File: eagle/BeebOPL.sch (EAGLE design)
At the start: 46 parts, among them IC1 LM324N, IC2 YM3014B, IC3 LM7805, IC5 74LS02N, IC6 YM3812, IC7 74LS04N, IC9 74HCT688N, J1 1 MHz Bus, J2 Feed-through, J3 3.5mm Jack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

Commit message: Further refined schematic
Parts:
- added C10, C11: 10nF, resistor:C-EU050-024X044
- JP3: value (none) -> AUDIO
- JP4: value (none) -> LED
- JP5: value (none) -> PWR
- S2: device SparkFun-Retired:JUMPER-2PTH -> SparkFun-Retired:SOLDERJUMPERTRACE-PTH
- S3: value JUMPER-3PTH -> REG; device SparkFun-Retired:JUMPER-3PTH -> YMSynth:J2
- TR1: value IRFD9024DIL -> IRFD9024; device YMSynth:IRFD9024DIL -> YMSynth:IRFD9024-OPTN
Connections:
- new net N$29: S3.1, TR1.S
- new net N$4: J4.PWR, JP5.4, TR1.D
- new net YM/IRQ: IC6./IRQ, S2.2
- net /IRQ: no longer IC6./IRQ, S2.2
- net GND: now also C10.2, C11.2
- net VCC: now also C10.1, C11.1; no longer J4.PWR, JP5.4, S3.1, TR1.D, TR1.S
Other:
- note removed: "Make sure signals pass through links correctly"
- moved on the sheet: C6, C7, S3

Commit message: Perfecting schematic
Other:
- note added: "Divide track to use voltage regulator"
- note removed: "Divide track to use power regulator"
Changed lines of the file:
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@@
 <grid distance="0.05" unitdist="inch" unit="inch" style="lines" multiple="1" display="no" altdistance="0.01" altunitdist="inch" altunit="inch"/>
 <layers>
-<layer number="1" name="Top" color="4" fill="1" visible="yes" active="no"/>
-<layer number="16" name="Bottom" color="1" fill="1" visible="yes" active="no"/>
-<layer number="17" name="Pads" color="2" fill="1" visible="yes" active="no"/>
-<layer number="18" name="Vias" color="2" fill="1" visible="yes" active="no"/>
-<layer number="19" name="Unrouted" color="6" fill="1" visible="yes" active="no"/>
-<layer number="20" name="Dimension" color="15" fill="1" visible="yes" active="no"/>
-<layer number="21" name="tPlace" color="7" fill="1" visible="yes" active="no"/>
-<layer number="22" name="bPlace" color="7" fill="1" visible="yes" active="no"/>
-<layer number="23" name="tOrigins" color="15" fill="1" visible="yes" active="no"/>
-<layer number="24" name="bOrigins" color="15" fill="1" visible="yes" active="no"/>
-<layer number="25" name="tNames" color="7" fill="1" visible="yes" active="no"/>
-<layer number="26" name="bNames" color="7" fill="1" visible="yes" active="no"/>
-<layer number="27" name="tValues" color="7" fill="1" visible="yes" active="no"/>
-<layer number="28" name="bValues" color="7" fill="1" visible="yes" active="no"/>
+<layer number="1" name="Top" color="4" fill="1" visible="no" active="no"/>
+<layer number="16" name="Bottom" color="1" fill="1" visible="no" active="no"/>
+<layer number="17" name="Pads" color="2" fill="1" visible="no" active="no"/>
+<layer number="18" name="Vias" color="2" fill="1" visible="no" active="no"/>
+<layer number="19" name="Unrouted" color="6" fill="1" visible="no" active="no"/>
+<layer number="20" name="Dimension" color="15" fill="1" visible="no" active="no"/>
+<layer number="21" name="tPlace" color="7" fill="1" visible="no" active="no"/>
+<layer number="22" name="bPlace" color="7" fill="1" visible="no" active="no"/>
+<layer number="23" name="tOrigins" color="15" fill="1" visible="no" active="no"/>
+<layer number="24" name="bOrigins" color="15" fill="1" visible="no" active="no"/>
+<layer number="25" name="tNames" color="7" fill="1" visible="no" active="no"/>
+<layer number="26" name="bNames" color="7" fill="1" visible="no" active="no"/>
+<layer number="27" name="tValues" color="7" fill="1" visible="no" active="no"/>
+<layer number="28" name="bValues" color="7" fill="1" visible="no" active="no"/>
 <layer number="29" name="tStop" color="7" fill="3" visible="no" active="no"/>
 <layer number="30" name="bStop" color="7" fill="6" visible="no" active="no"/>
@@
 <layer number="35" name="tGlue" color="7" fill="4" visible="no" active="no"/>
 <layer number="36" name="bGlue" color="7" fill="5" visible="no" active="no"/>
-<layer number="37" name="tTest" color="7" fill="1" visible="yes" active="no"/>
-<layer number="38" name="bTest" color="7" fill="1" visible="yes" active="no"/>
+<layer number="37" name="tTest" color="7" fill="1" visible="no" active="no"/>
+<layer number="38" name="bTest" color="7" fill="1" visible="no" active="no"/>
 <layer number="39" name="tKeepout" color="4" fill="11" visible="no" active="no"/>
 <layer number="40" name="bKeepout" color="1" fill="11" visible="no" active="no"/>
@@
 <layer number="44" name="Drills" color="7" fill="1" visible="no" active="no"/>
 <layer number="45" name="Holes" color="7" fill="1" visible="no" active="no"/>
-<layer number="46" name="Milling" color="3" fill="1" visible="yes" active="no"/>
-<layer number="47" name="Measures" color="7" fill="1" visible="yes" active="no"/>
-<layer number="48" name="Document" color="7" fill="1" visible="yes" active="no"/>
-<layer number="49" name="Reference" color="7" fill="1" visible="yes" active="no"/>
-<layer number="50" name="dxf" color="7" fill="1" visible="yes" active="no"/>
-<layer number="51" name="tDocu" color="7" fill="1" visible="yes" active="no"/>
-<layer number="52" name="bDocu" color="7" fill="1" visible="yes" active="no"/>
-<layer number="53" name="tGND_GNDA" color="7" fill="9" visible="yes" active="no"/>
-<layer number="54" name="bGND_GNDA" color="1" fill="9" visible="yes" active="no"/>
-<layer number="56" name="wert" color="7" fill="1" visible="yes" active="no"/>
-<layer number="57" name="tCAD" color="7" fill="1" visible="yes" active="no"/>
-<layer number="59" name="tCarbon" color="7" fill="1" visible="yes" active="no"/>
-<layer number="60" name="bCarbon" color="7" fill="1" visible="yes" active="no"/>
+<layer number="46" name="Milling" color="3" fill="1" visible="no" active="no"/>
+<layer number="47" name="Measures" color="7" fill="1" visible="no" active="no"/>
+<layer number="48" name="Document" color="7" fill="1" visible="no" active="no"/>
+<layer number="49" name="Reference" color="7" fill="1" visible="no" active="no"/>
+<layer number="50" name="dxf" color="7" fill="1" visible="no" active="no"/>
+<layer number="51" name="tDocu" color="7" fill="1" visible="no" active="no"/>
+<layer number="52" name="bDocu" color="7" fill="1" visible="no" active="no"/>
+<layer number="53" name="tGND_GNDA" color="7" fill="9" visible="no" active="no"/>
+<layer number="54" name="bGND_GNDA" color="1" fill="9" visible="no" active="no"/>
+<layer number="56" name="wert" color="7" fill="1" visible="no" active="no"/>
+<layer number="57" name="tCAD" color="7" fill="1" visible="no" active="no"/>
+<layer number="59" name="tCarbon" color="7" fill="1" visible="no" active="no"/>
+<layer number="60" name="bCarbon" color="7" fill="1" visible="no" active="no"/>
 <layer number="90" name="Modules" color="5" fill="1" visible="yes" active="yes"/>
 <layer number="91" name="Nets" color="2" fill="1" visible="yes" active="yes"/>
@@
 <text x="-175.26" y="-175.26" size="10.16" layer="97" font="vector">DATE: 29 Sept 2016</text>
 <text x="-88.9" y="-50.8" size="1.778" layer="97">Divide track to use
-power regulator</text>
+voltage regulator</text>
 <text x="-97.79" y="-109.22" size="1.778" layer="97">Divide track to use
 power MOSFET</text>

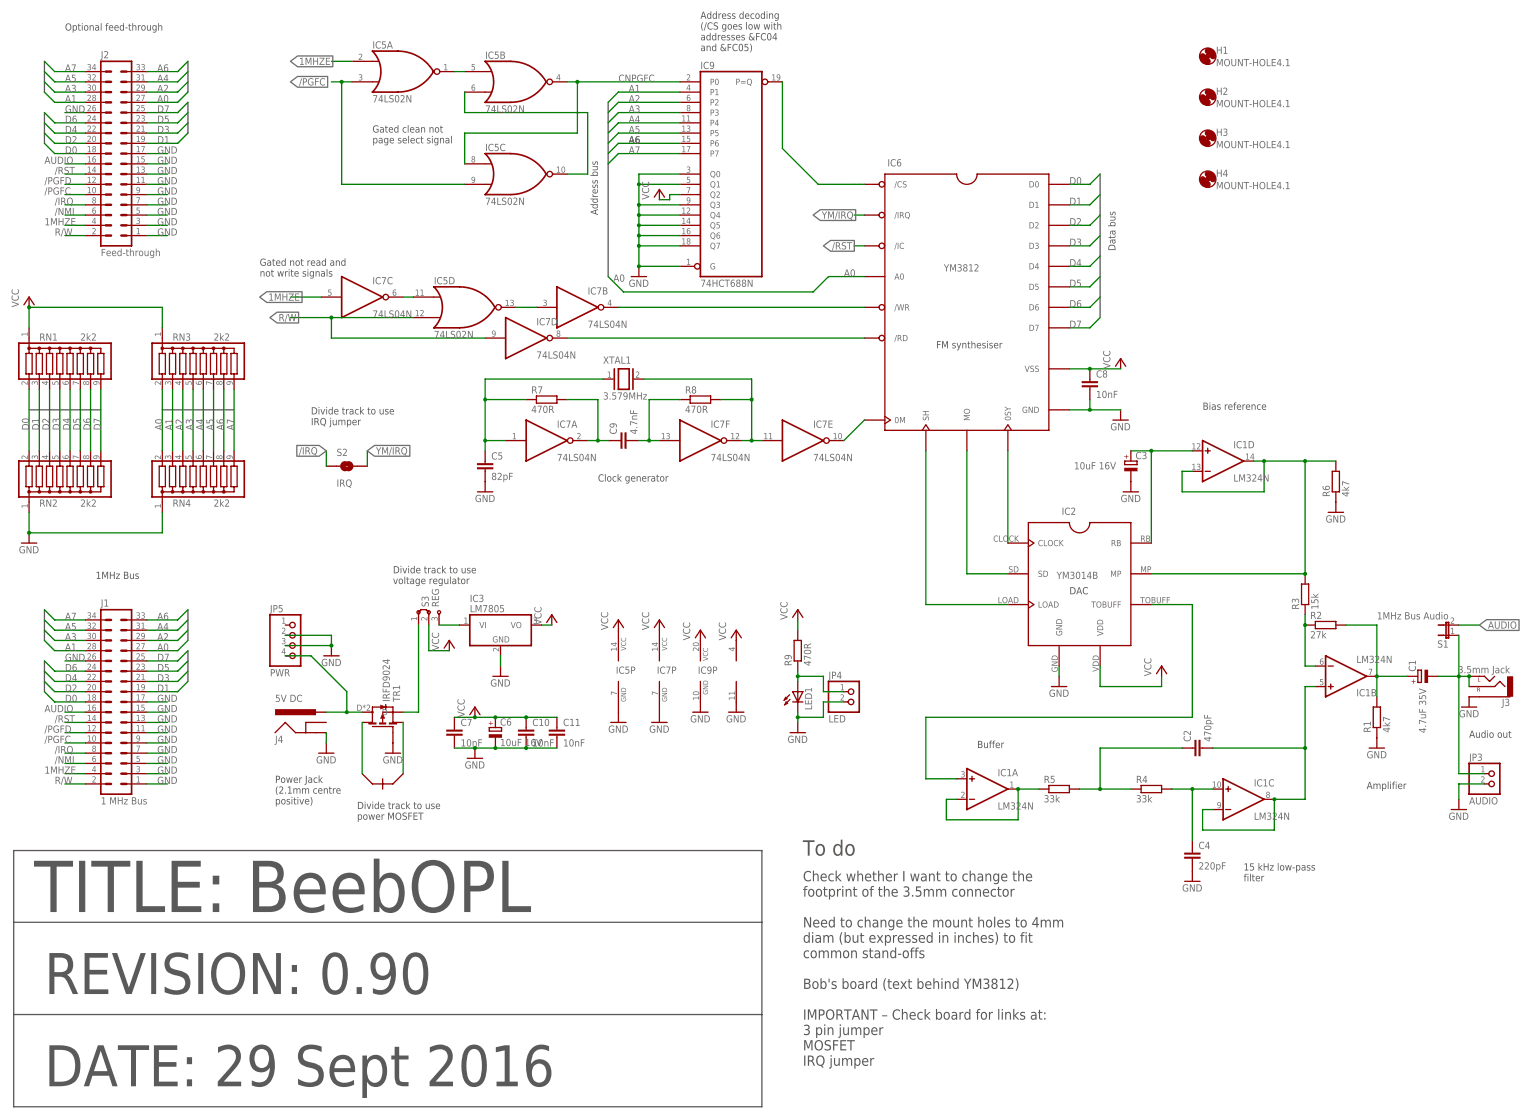
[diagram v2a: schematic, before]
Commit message: More sophisticated power section
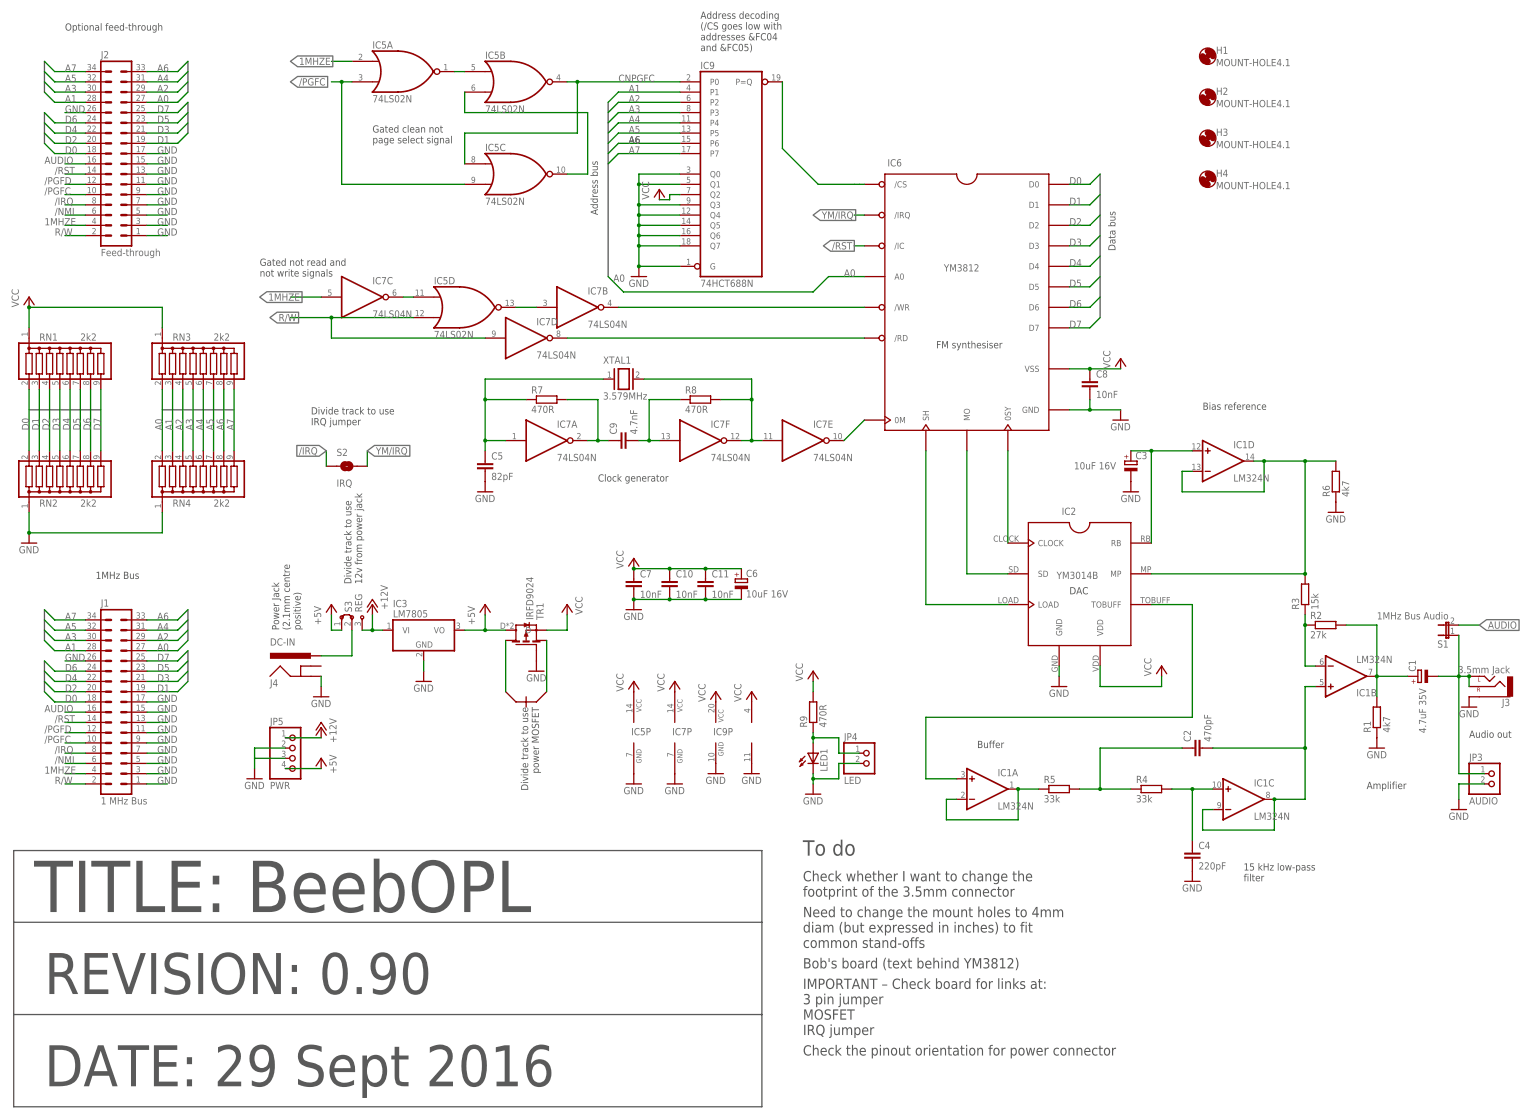
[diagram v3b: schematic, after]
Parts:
- J4: value 5V DC -> DC-IN
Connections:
- removed net N$27: IC3.VI, S3.3
- new net +12V: IC3.VI, JP5.1, S3.3
- new net +5V: IC3.VO, JP5.4, S3.1, TR1.D
- net GND: no longer JP5.2, JP5.3
- net N$29: now also JP5.2, JP5.3; no longer S3.1, TR1.S
- net N$4: now also S3.2; no longer JP5.4, TR1.D
- net VCC: now also TR1.S; no longer IC3.VO, S3.2
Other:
- note added: "Check the pinout orientation for power connector"
- note added: "Divide track to use 12v from power jack"
- note removed: "Divide track to use voltage regulator"
- moved on the sheet: C10, C11, C6, C7, IC3, IC5P, IC7P, IC9P, J4, JP4, JP5, LED1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

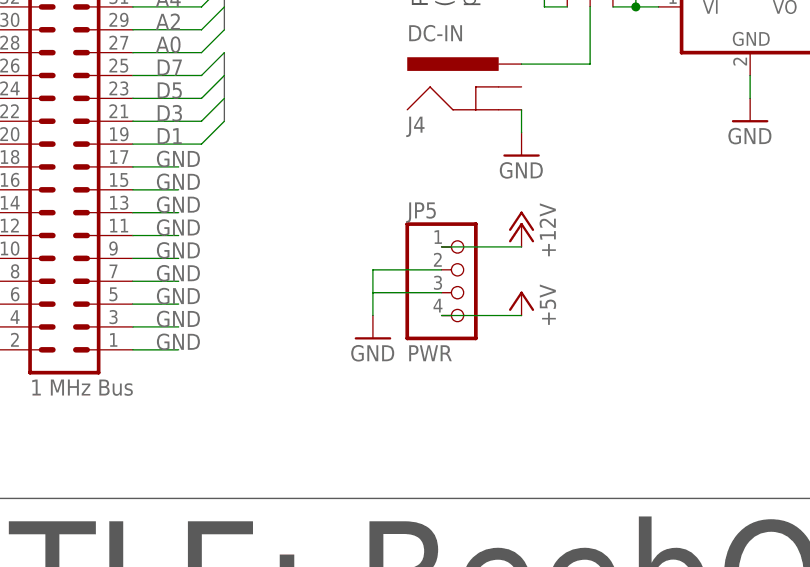
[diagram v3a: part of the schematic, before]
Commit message: Assigned net classes
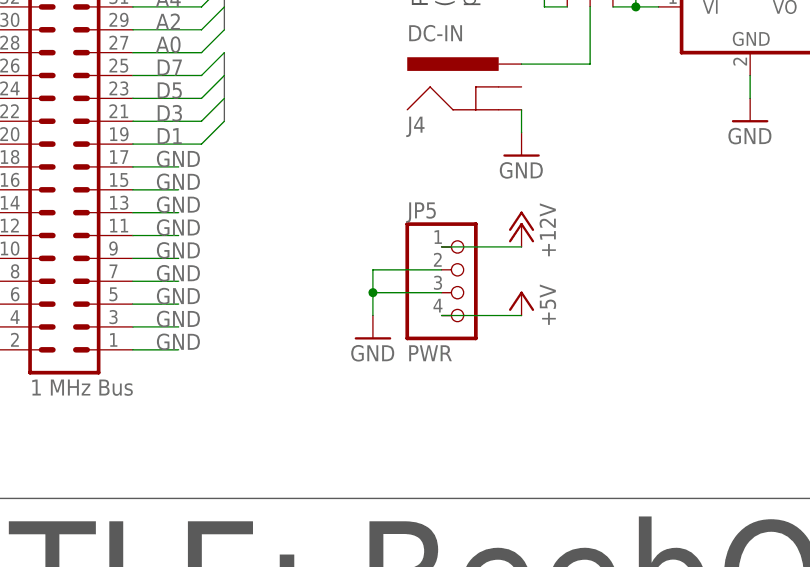
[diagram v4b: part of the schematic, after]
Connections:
- net N$17 renamed AUDIO_OUT
- net N$4 renamed DC
- removed net N$29: JP5.2, JP5.3
- net GND: now also JP5.2, JP5.3
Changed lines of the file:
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@@
 <pinref part="GND19" gate="1" pin="GND"/>
 <wire x1="-123.19" y1="-93.98" x2="-123.19" y2="-96.52" width="0.1524" layer="91"/>
+<pinref part="JP5" gate="A" pin="3"/>
+<wire x1="-123.19" y1="-93.98" x2="-115.57" y2="-93.98" width="0.1524" layer="91"/>
+<pinref part="JP5" gate="A" pin="2"/>
+<wire x1="-115.57" y1="-91.44" x2="-123.19" y2="-91.44" width="0.1524" layer="91"/>
+<wire x1="-123.19" y1="-93.98" x2="-123.19" y2="-91.44" width="0.1524" layer="91"/>
+<junction x="-123.19" y="-93.98"/>
 </segment>
 <segment>
@@
 </segment>
 </net>
-<net name="N$17" class="2">
+<net name="AUDIO_OUT" class="2">
 <segment>
 <pinref part="C1" gate="G$1" pin="-"/>
@@
 </segment>
 </net>
-<net name="+12V" class="0">
+<net name="+12V" class="1">
 <segment>
 <pinref part="JP5" gate="A" pin="1"/>
@@
 </segment>
 </net>
-<net name="N$4" class="0">
+<net name="DC" class="1">
 <segment>
 <pinref part="J4" gate="G$1" pin="PWR"/>
@@
 </segment>
 </net>
-<net name="N$29" class="0">
-<segment>
-<pinref part="JP5" gate="A" pin="2"/>
-<wire x1="-115.57" y1="-91.44" x2="-123.19" y2="-91.44" width="0.1524" layer="91"/>
-<pinref part="JP5" gate="A" pin="3"/>
-<wire x1="-115.57" y1="-93.98" x2="-123.19" y2="-93.98" width="0.1524" layer="91"/>
-<wire x1="-123.19" y1="-91.44" x2="-123.19" y2="-93.98" width="0.1524" layer="91"/>
-</segment>
-</net>

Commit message: Initial board layout
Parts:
- removed H1, H2, H3, H4: MOUNT-HOLE4.1, holes:MOUNT-HOLE4.1
- JP3, JP4: device pinhead:PINHD-1X2/90 -> pinhead:PINHD-1X2
- JP5: device pinhead:PINHD-1X4/90 -> pinhead:PINHD-1X4
- LED1: value (none) -> LED
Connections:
- net A1: now also IC9A.P4; no longer IC9A.P1
- net A2: now also IC9A.P3; no longer IC9A.P2
- net A3: now also IC9A.P5; no longer IC9A.P3
- net A4: now also IC9A.P2; no longer IC9A.P4
- net A5: now also IC9A.P6; no longer IC9A.P5
- net A6: now also IC9A.P1; no longer IC9A.P6
- net GND: now also IC9A.Q2; no longer IC9A.Q3
- net VCC: now also IC9A.Q3; no longer IC9A.Q2
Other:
- note added: "Check that sockets etc fit with overhang"
- note removed: "Need to change the mount holes to 4mm diam (but expressed in inches) to fit common stand-offs"

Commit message: Routing signals
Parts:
- C10, C11: value 10nF -> 100nF
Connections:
- net GND: now also J4.GNDBREAK
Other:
- note added: "Put arrows at track cut points"
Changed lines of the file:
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@@
 <setting verticaltext="up"/>
 </settings>
-<grid distance="0.05" unitdist="inch" unit="inch" style="lines" multiple="1" display="no" altdistance="0.01" altunitdist="inch" altunit="inch"/>
+<grid distance="0.1" unitdist="inch" unit="inch" style="lines" multiple="1" display="no" altdistance="0.01" altunitdist="inch" altunit="inch"/>
 <layers>
 <layer number="1" name="Top" color="4" fill="1" visible="no" active="no"/>
@@
 <part name="P+9" library="supply1" deviceset="VCC" device=""/>
 <part name="JP5" library="pinhead" deviceset="PINHD-1X4" device="" value="PWR"/>
-<part name="C10" library="resistor" deviceset="C-EU" device="050-024X044" value="10nF"/>
-<part name="C11" library="resistor" deviceset="C-EU" device="050-024X044" value="10nF"/>
+<part name="C10" library="resistor" deviceset="C-EU" device="050-024X044" value="100nF"/>
+<part name="C11" library="resistor" deviceset="C-EU" device="050-024X044" value="100nF"/>
 <part name="S2" library="SparkFun-Retired" deviceset="SOLDERJUMPER" device="TRACE-PTH" value="IRQ"/>
 <part name="S3" library="YMSynth" deviceset="J2" device="" value="REG"/>
@@
 <text x="12.7" y="-154.94" size="2.54" layer="97">Check the pinout orientation for power connector</text>
 <text x="12.7" y="-160.02" size="2.54" layer="97">Check that sockets etc fit with overhang</text>
+<text x="12.7" y="-165.1" size="2.54" layer="97">Put arrows at track cut points</text>
 </plain>
 <instances>
@@
 <wire x1="-106.68" y1="-73.66" x2="-106.68" y2="-76.2" width="0.1524" layer="91"/>
 <pinref part="GND13" gate="1" pin="GND"/>
-</segment>
-<segment>
+<pinref part="J4" gate="G$1" pin="GNDBREAK"/>
+<wire x1="-106.68" y1="-73.66" x2="-106.68" y2="-71.12" width="0.1524" layer="91"/>
+<junction x="-106.68" y="-73.66"/>
+</segment>
+<segment>

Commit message: Finished routing
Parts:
- S2: device SparkFun-Retired:SOLDERJUMPERTRACE-PTH -> YMSynth:JUMPER-2PTH
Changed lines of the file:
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@@
 </class>
 <class number="1" name="pwr" width="1.016" drill="0">
-<clearance class="1" value="0.1524"/>
+<clearance class="1" value="0.254"/>
 </class>
 <class number="2" name="audio" width="1.016" drill="0">
-<clearance class="2" value="0.1524"/>
+<clearance class="2" value="0.254"/>
 </class>
 <class number="3" name="gnd" width="1.016" drill="0">
-<clearance class="3" value="0.1524"/>
+<clearance class="3" value="0.254"/>
 </class>
 </classes>
@@
 <part name="C10" library="resistor" deviceset="C-EU" device="050-024X044" value="100nF"/>
 <part name="C11" library="resistor" deviceset="C-EU" device="050-024X044" value="100nF"/>
-<part name="S2" library="SparkFun-Retired" deviceset="SOLDERJUMPER" device="TRACE-PTH" value="IRQ"/>
+<part name="S2" library="YMSynth" deviceset="JUMPER-2" device="PTH" value="IRQ"/>
 <part name="S3" library="YMSynth" deviceset="J2" device="" value="REG"/>
 <part name="TR1" library="YMSynth" deviceset="IRFD9024-OPTN" device="" value="IRFD9024"/>
@@
 <segment>
 <pinref part="S2" gate="1" pin="1"/>
-<wire x1="-105.41" y1="-21.59" x2="-105.41" y2="-17.78" width="0.1524" layer="91"/>
-<label x="-105.41" y="-17.78" size="1.778" layer="95" rot="MR0" xref="yes"/>
+<wire x1="-100.33" y1="-24.13" x2="-106.68" y2="-24.13" width="0.1524" layer="91"/>
+<label x="-106.68" y="-24.13" size="1.778" layer="95" rot="MR0" xref="yes"/>
 </segment>
 </net>
@@
 <segment>
 <pinref part="S2" gate="1" pin="2"/>
-<wire x1="-95.25" y1="-21.59" x2="-95.25" y2="-17.78" width="0.1524" layer="91"/>
-<label x="-95.25" y="-17.78" size="1.778" layer="95" xref="yes"/>
-</segment>
-</net>
+<wire x1="-97.79" y1="-24.13" x2="-87.63" y2="-24.13" width="0.1524" layer="91"/>
+<label x="-87.63" y="-24.13" size="1.778" layer="95" xref="yes"/>
+</segment>
+</net>
